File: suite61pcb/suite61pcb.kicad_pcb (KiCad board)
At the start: 2 copper layers, 189.6 x 115.8 mm, 99 parts, among them J1 Battery JST, J2 OLED, J3 FFC_Receiver, SW1 MX_SW_HS, SW10 MX_SW_HS, SW11 MX_SW_HS, SW12 MX_SW_HS, SW13 MX_SW, SW14 MX_SW, SW15 MX_SW_HS, SW16 MX_SW_HS, SW17 MX_SW_HS, SW18 MX_SW_HS, SW19 MX_SW_HS, SW2 MX_SW_HS, SW20 Reset_Button, SW21 MX_SW, SW22 MX_SW, SW23 MX_SW_HS, SW24 MX_SW_HS, SW25 MX_SW_HS, SW26 MX_SW_HS, SW27 MX_SW_HS, SW28 MX_SW_HS, SW29 MX_SW_HS, SW3 MX_SW_HS, SW30 MX_SW_HS, SW31 MX_SW_HS, SW32 MX_SW_HS, SW33 MX_SW_HS, SW34 MX_SW_HS, SW35 MX_SW_HS, SW36 MX_SW_HS, SW37 RotaryEncoder_Switch, SW4 MX_SW_HS, SW5 MX_SW_HS, SW6 MX_SW_HS, SW7 MX_SW_HS, SW8 MX_SW_HS, SW9 MX_SW_HS, U1 nice_nano

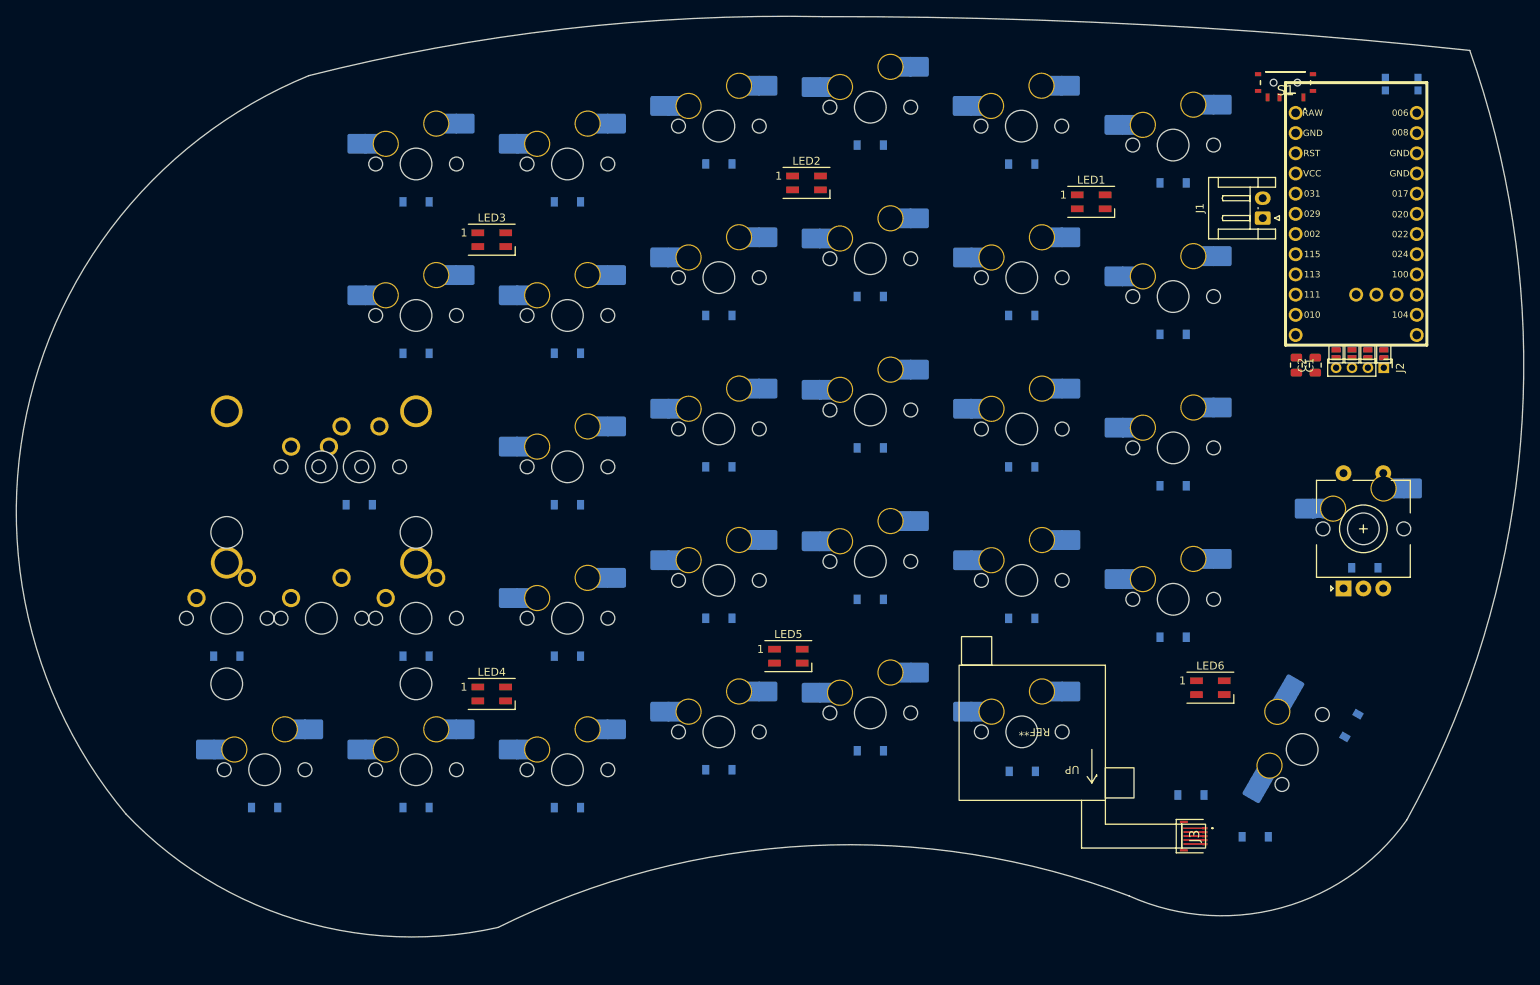
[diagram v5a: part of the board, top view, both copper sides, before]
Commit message: create edge outline
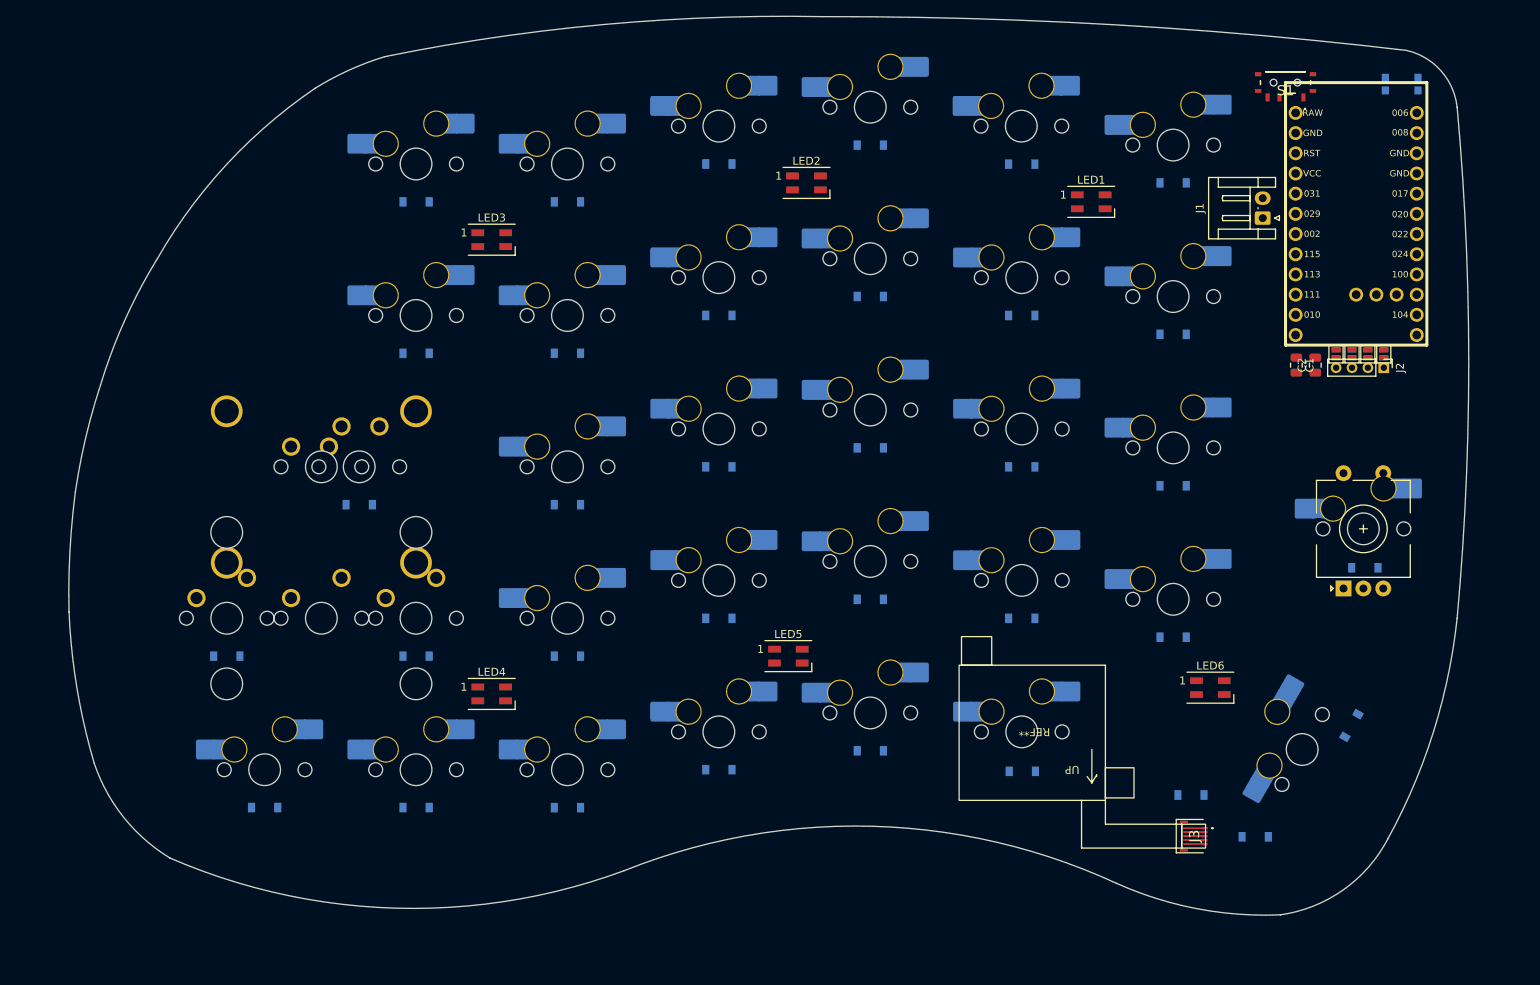
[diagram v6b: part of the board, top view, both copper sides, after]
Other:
- board size 189.6 x 115.8 mm -> 176.1 x 113.1 mm
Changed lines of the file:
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@@
     (fp_arc (start -7 -6.5) (mid -6.853553 -6.853553) (end -6.5 -7) (layer "Eco2.User") (width 0.05))
     (fp_arc (start 6.997236 6.498884) (mid 6.850756 6.852405) (end 6.497236 6.998884) (layer "Eco2.User") (width 0.05))
-    (fp_arc (start 14.780039 -5.999999) (mid 15.133596 -5.853568) (end 15.280039 -5.499999) (layer "Eco2.User") (width 0.05))
+    (fp_arc (start 14.780039 -5.999999) (mid 15.133631 -5.853574) (end 15.280039 -5.499999) (layer "Eco2.User") (width 0.05))
     (fp_arc (start -9.03125 -5.999999) (mid -8.677697 -5.853552) (end -8.53125 -5.499999) (layer "Eco2.User") (width 0.05))
-    (fp_arc (start 9.03125 8.000001) (mid 8.677664 7.853572) (end 8.53125 7.500001) (layer "Eco2.User") (width 0.05))
+    (fp_arc (start 9.03125 8.000001) (mid 8.677699 7.853566) (end 8.53125 7.500001) (layer "Eco2.User") (width 0.05))
     (fp_arc (start -8.53125 7.500001) (mid -8.677697 7.853554) (end -9.03125 8.000001) (layer "Eco2.User") (width 0.05))
     (fp_arc (start 6.5 -7) (mid 6.853553 -6.853553) (end 7 -6.5) (layer "Eco2.User") (width 0.05))
-    (fp_arc (start 8.53125 -5.499999) (mid 8.677738 -5.853509) (end 9.03125 -5.999999) (layer "Eco2.User") (width 0.05))
-    (fp_arc (start 15.28125 7.500001) (mid 15.134777 7.853542) (end 14.78125 8.000001) (layer "Eco2.User") (width 0.05))
+    (fp_arc (start 8.53125 -5.499999) (mid 8.677741 -5.853506) (end 9.03125 -5.999999) (layer "Eco2.User") (width 0.05))
+    (fp_arc (start 15.28125 7.500001) (mid 15.134771 7.853507) (end 14.78125 8.000001) (layer "Eco2.User") (width 0.05))
     (fp_arc (start -6.5 7) (mid -6.853553 6.853553) (end -7 6.5) (layer "Eco2.User") (width 0.05))
     (fp_arc (start -15.28125 -5.499999) (mid -15.134803 -5.853552) (end -14.78125 -5.999999) (layer "Eco2.User") (width 0.05))
@@
     (fp_arc (start -9.03125 -5.999999) (mid -8.677697 -5.853552) (end -8.53125 -5.499999) (layer "Eco2.User") (width 0.05))
     (fp_arc (start -7 -6.5) (mid -6.853553 -6.853553) (end -6.5 -7) (layer "Eco2.User") (width 0.05))
-    (fp_arc (start 8.53125 -5.499999) (mid 8.677738 -5.853509) (end 9.03125 -5.999999) (layer "Eco2.User") (width 0.05))
+    (fp_arc (start 8.53125 -5.499999) (mid 8.677741 -5.853506) (end 9.03125 -5.999999) (layer "Eco2.User") (width 0.05))
     (fp_arc (start -14.78125 8.000001) (mid -15.134803 7.853554) (end -15.28125 7.500001) (layer "Eco2.User") (width 0.05))
     (fp_arc (start -8.53125 7.500001) (mid -8.677697 7.853554) (end -9.03125 8.000001) (layer "Eco2.User") (width 0.05))
-    (fp_arc (start 15.28125 7.500001) (mid 15.134777 7.853542) (end 14.78125 8.000001) (layer "Eco2.User") (width 0.05))
-    (fp_arc (start 9.03125 8.000001) (mid 8.677664 7.853572) (end 8.53125 7.500001) (layer "Eco2.User") (width 0.05))
+    (fp_arc (start 15.28125 7.500001) (mid 15.134771 7.853507) (end 14.78125 8.000001) (layer "Eco2.User") (width 0.05))
+    (fp_arc (start 9.03125 8.000001) (mid 8.677699 7.853566) (end 8.53125 7.500001) (layer "Eco2.User") (width 0.05))
     (fp_arc (start 6.5 -7) (mid 6.853553 -6.853553) (end 7 -6.5) (layer "Eco2.User") (width 0.05))
-    (fp_arc (start 14.780039 -5.999999) (mid 15.133596 -5.853568) (end 15.280039 -5.499999) (layer "Eco2.User") (width 0.05))
+    (fp_arc (start 14.780039 -5.999999) (mid 15.133631 -5.853574) (end 15.280039 -5.499999) (layer "Eco2.User") (width 0.05))
     (fp_arc (start 6.997236 6.498884) (mid 6.850756 6.852405) (end 6.497236 6.998884) (layer "Eco2.User") (width 0.05))
     (fp_line (start -7 -7) (end -7 7) (layer "F.CrtYd") (width 0.05))
@@
     (fp_arc (start -4.864824 3.20022) (mid -4.718377 2.846667) (end -4.364824 2.70022) (layer "B.SilkS") (width 0.15))
     (fp_arc (start 2.494322 0.86022) (mid 1.670693 2.183637) (end 0.2 2.70022) (layer "B.SilkS") (width 0.15))
-    (fp_arc (start 6.085176 4.75022) (mid 5.499393 6.164437) (end 4.085176 6.75022) (layer "B.SilkS") (width 0.15))
+    (fp_arc (start 6.085176 4.75022) (mid 5.499392 6.164435) (end 4.085176 6.75022) (layer "B.SilkS") (width 0.15))
     (fp_line (start 9.525 -9.525) (end -9.525 -9.525) (layer "Dwgs.User") (width 0.12))
     (fp_line (start -9.525 -9.525) (end -9.525 9.525) (layer "Dwgs.User") (width 0.12))
@@
     (fp_line (start -4.864824 3.87022) (end -4.864824 2.70022) (layer "B.CrtYd") (width 0.05))
     (fp_arc (start 2.494322 0.86022) (mid 1.670502 2.183399) (end 0.2 2.70022) (layer "B.CrtYd") (width 0.05))
-    (fp_arc (start 6.085176 4.75022) (mid 5.499393 6.164437) (end 4.085176 6.75022) (layer "B.CrtYd") (width 0.05))
+    (fp_arc (start 6.085176 4.75022) (mid 5.499392 6.164435) (end 4.085176 6.75022) (layer "B.CrtYd") (width 0.05))
     (fp_line (start 7 -7) (end -7 -7) (layer "F.CrtYd") (width 0.05))
     (fp_line (start 7 7) (end 7 -7) (layer "F.CrtYd") (width 0.05))
@@
     )
   )
-  (gr_arc (start 77.7875 29.36875) (mid 109.85027 23.503504) (end 142.407734 21.943379) (layer "Edge.Cuts") (width 0.1))
-  (gr_arc (start 101.6 136.525) (mid 140.87251 126.240817) (end 180.975 132.55625) (layer "Edge.Cuts") (width 0.1))
-  (gr_arc (start 223.8375 26.19375) (mid 230.2357 75.462248) (end 215.9 123.03125) (layer "Edge.Cuts") (width 0.1))
-  (gr_arc (start 142.407734 21.943379) (mid 183.180106 22.967167) (end 223.8375 26.19375) (layer "Edge.Cuts") (width 0.1))
-  (gr_arc (start 101.6 136.525) (mid 76.2977 135.56535) (end 54.76875 122.2375) (layer "Edge.Cuts") (width 0.1))
-  (gr_arc (start 54.76875 122.2375) (mid 42.729925 69.966391) (end 77.7875 29.36875) (layer "Edge.Cuts") (width 0.1))
-  (gr_arc (start 215.9 123.03125) (mid 200.144306 134.052039) (end 180.975 132.55625) (layer "Edge.Cuts") (width 0.1))
+  (gr_arc (start 87.3125 26.9875) (mid 114.72134 22.949627) (end 142.407734 21.943379) (layer "Edge.Cuts") (width 0.1))
+  (gr_arc (start 117.475 129.38125) (mid 148.594878 123.793501) (end 179.3875 130.96875) (layer "Edge.Cuts") (width 0.1))
+  (gr_arc (start 200.025 134.937499) (mid 189.474505 134.1582) (end 179.3875 130.96875) (layer "Edge.Cuts") (width 0.1))
+  (gr_arc (start 222.25 33.3375) (mid 223.712399 65.484375) (end 222.25 97.63125) (layer "Edge.Cuts") (width 0.1))
+  (gr_arc (start 51.59375 68.2625) (mid 54.656291 60.0958) (end 58.7375 52.3875) (layer "Edge.Cuts") (width 0.1))
+  (gr_arc (start 47.625 96.8375) (mid 47.734002 89.281724) (end 48.41875 81.75625) (layer "Edge.Cuts") (width 0.1))
+  (gr_arc (start 215.9 26.19375) (mid 220.214435 28.752794) (end 222.25 33.3375) (layer "Edge.Cuts") (width 0.1))
+  (gr_arc (start 142.407734 21.943379) (mid 179.217334 22.971178) (end 215.9 26.19375) (layer "Edge.Cuts") (width 0.1))
+  (gr_arc (start 78.58125 30.95625) (mid 82.819052 28.690663) (end 87.3125 26.9875) (layer "Edge.Cuts") (width 0.1))
+  (gr_arc (start 117.475 129.38125) (mid 88.746849 134.100947) (end 60.325 127.79375) (layer "Edge.Cuts") (width 0.1))
+  (gr_arc (start 48.41875 81.75625) (mid 49.71695 74.941304) (end 51.59375 68.2625) (layer "Edge.Cuts") (width 0.1))
+  (gr_arc (start 60.325 127.79375) (mid 54.50891 122.6835) (end 50.8 115.8875) (layer "Edge.Cuts") (width 0.1))
+  (gr_arc (start 58.7375 52.3875) (mid 67.441824 40.544518) (end 78.58125 30.95625) (layer "Edge.Cuts") (width 0.1))
+  (gr_arc (start 50.8 115.8875) (mid 48.628743 106.459793) (end 47.625 96.8375) (layer "Edge.Cuts") (width 0.1))
+  (gr_arc (start 222.25 97.63125) (mid 219.262748 111.955078) (end 213.51875 125.4125) (layer "Edge.Cuts") (width 0.1))
+  (gr_arc (start 213.51875 125.4125) (mid 207.921299 131.803351) (end 200.025 134.9375) (layer "Edge.Cuts") (width 0.1))
 )

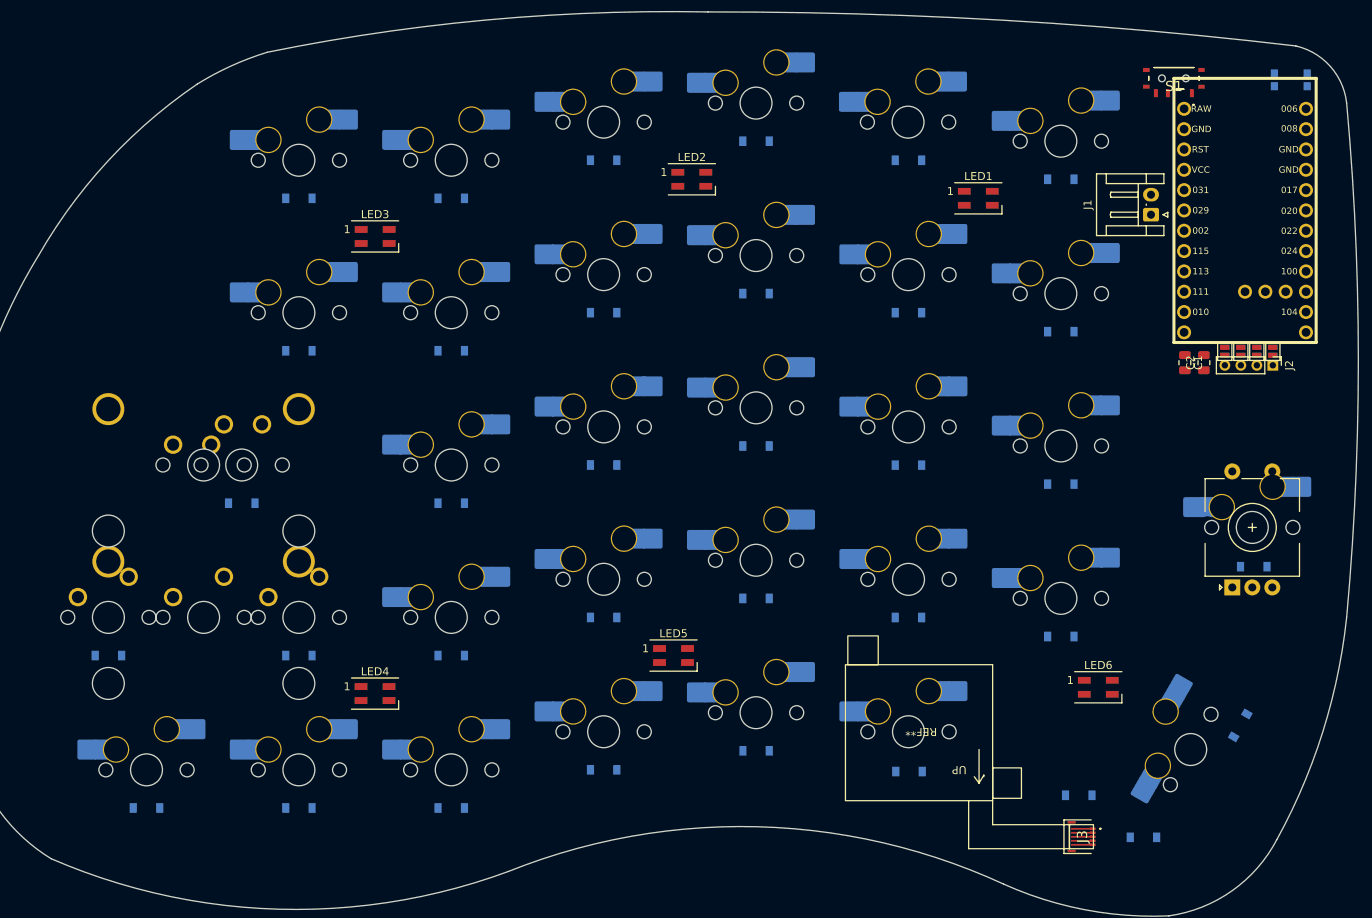
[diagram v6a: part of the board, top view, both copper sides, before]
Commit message: update pcb
check if oled header is right
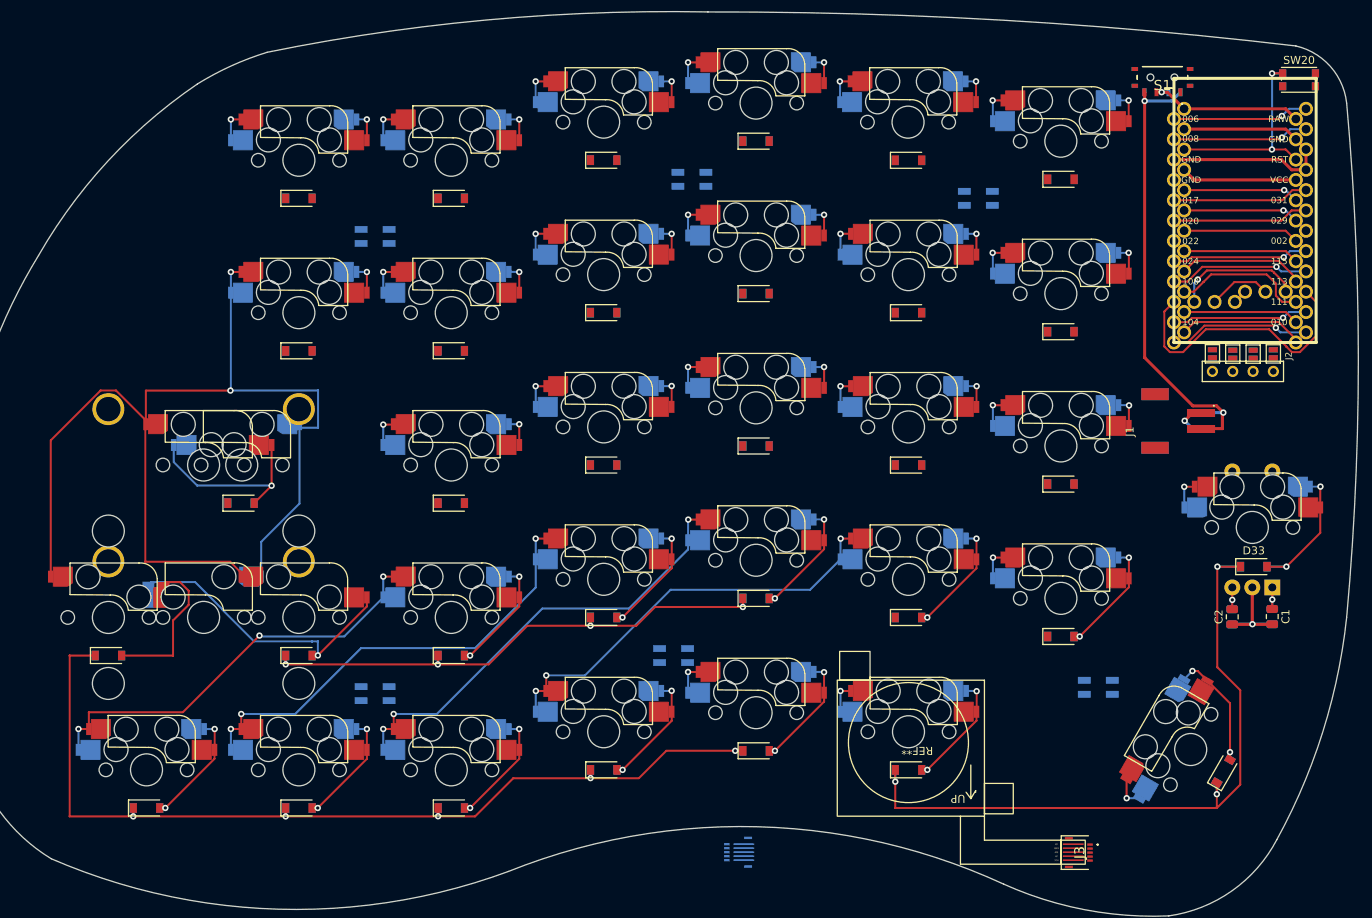
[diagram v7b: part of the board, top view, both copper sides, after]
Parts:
- removed the D31 at (188.8, 119.9)
- removed D34: 1N4148W, Diode_SMD:D_SOD-123
- added J3: FFC_Receiver, LIB_503480-0500:5034800500, B.Cu at (146.4, 127.0)
- added REF**: joycon joystick, suite61:joycon joystick, B.Cu at (158.2, 111.5)
- D1, D10, D11, D12, D13, D14, D15, D16, D17, D18, D19, D2, D20, D21, D22, D23, D24, D25, D26, D27, D28, D29, D3, D30, D4, D5, D6, D7, D8, D9: footprint Diode_SMD:D_SOD-123 -> suite61:D_SOD-123
- D31: renamed from D32; footprint Diode_SMD:D_SOD-123 -> suite61:D_SOD-123
- D32: renamed from D33; footprint Diode_SMD:D_SOD-123 -> suite61:D_SOD-123
- D33: renamed from D35; footprint Diode_SMD:D_SOD-123 -> suite61:D_SOD-123; moved to F.Cu
- J1: footprint Connector_JST:JST_EH_S2B-EH_1x02_P2.50mm_Horizontal -> suite61:JST_S2B-PH-SM4-TB
- J2: footprint Connector_PinHeader_2.00mm:PinHeader_1x04_P2.00mm_Vertical -> SofleKeyboard-footprint:OLED_4Pin
- JP1, JP2, JP3, JP4, LED1, LED2, LED3, LED4, LED5, LED6, SW37: moved to B.Cu
- JP5, JP6, JP7, JP8, SW20: moved to F.Cu
- REF**: value 2-way joystick switch -> joycon joystick; footprint suite61:2-way joystick switch -> suite61:joycon joystick
- SW1, SW10, SW11, SW12, SW15, SW16, SW17, SW18, SW19, SW2, SW23, SW24, SW25, SW26, SW27, SW29, SW3, SW30, SW31, SW32, SW33, SW4, SW5, SW6, SW8, SW9: footprint marbastlib-mx:SW_MX_HS_1u -> suite61:CherryMX_Hotswap; moved to F.Cu
- SW13: footprint marbastlib-mx:SW_MX_1.75u -> suite61:SW_MX_HS_1.75u_1side; moved to B.Cu
- SW14: footprint suite61:SW_MX_P_2.25u -> suite61:STAB_MX_P__HS_2.25u_1side
- SW21: footprint suite61:SW_MX_P_2.25u -> suite61:STAB_MX_P__HS_2.25u_1side; moved to B.Cu
- SW22: footprint marbastlib-mx:SW_MX_1u -> suite61:CherryMX_Hotswap
- SW28: footprint marbastlib-mx:SW_MX_HS_1u -> suite61:CherryMX_Hotswap_1.5; moved to F.Cu
- SW34: footprint marbastlib-mx:SW_MX_1.5u -> suite61:CherryMX_Hotswap
- SW35, SW7: footprint marbastlib-mx:SW_MX_HS_1.5u -> suite61:CherryMX_Hotswap_1.5; moved to F.Cu
- SW36: footprint marbastlib-mx:SW_MX_HS_1u -> suite61:CherryMX_Hotswap
- U1: footprint nice-nano-kicad-master:nice_nano -> suite61:nice_nano
- moved SW34 101.0 mm to (167.5, 111.9)
- moved D31 101.0 mm to (167.5, 116.7)
- moved C1 33.6 mm to (212.9, 97.5)
- moved C2 32.0 mm to (207.9, 97.5)
- moved J1 26.5 mm to (204.1, 73.1)
- moved SW28 19.6 mm to (67.5, 97.6), turned to 0 degrees
- moved D25 19.6 mm to (67.5, 102.4)
- moved SW31 19.6 mm to (110.3, 116.7), turned to 0 degrees
- moved D28 19.6 mm to (110.3, 121.4)
- moved D30 19.3 mm to (148.4, 114.3)
- moved SW33 19.2 mm to (148.4, 109.5), turned to 0 degrees
- moved D29 19.2 mm to (129.4, 116.7)
- moved SW32 19.2 mm to (129.4, 111.9), turned to 0 degrees
- moved D26 19.0 mm to (72.2, 121.4)
- moved SW29 19.0 mm to (72.2, 116.7), turned to 0 degrees
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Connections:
- J3 pad 3: Net-(D34-Pad2) -> JSBTN
- U1 pad 2: unconnected-(U1-Pad2) -> DATA
- U1 pad 31: Enc0 -> JSBTN
- U1 pad 33: unconnected-(U1-Pad33) -> Enc0
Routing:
- net col5: track 0.00 -> 155.0 mm, vias 0 -> 4
- net row4: track 0.00 -> 135.0 mm, vias 0 -> 5
- net row5: track 0.00 -> 105.4 mm, vias 0 -> 3
- net col3: track 0.00 -> 102.9 mm, vias 0 -> 6
- net col2: track 0.00 -> 89.3 mm, vias 0 -> 8
- net row3: track 0.00 -> 86.0 mm, vias 0 -> 4
- net col1: track 0.00 -> 85.9 mm, vias 0 -> 8
- net col4: track 0.00 -> 81.5 mm, vias 0 -> 7
- net GND: track 0.00 -> 58.9 mm, vias 0 -> 2
- net Net-(J1-Pad2): track 0.00 -> 57.4 mm, vias 0 -> 2
- net Net-(D19-Pad2): track 0.00 -> 37.4 mm, vias 0 -> 1
- net RESET: track 0.00 -> 26.7 mm, vias 0 -> 2
- net Net-(D13-Pad2): track 0.00 -> 23.8 mm, vias 0 -> 1
- net col0: track 0.00 -> 23.5 mm, vias 0 -> 6
- net BATTERY: track 0.00 -> 19.7 mm, vias 0 -> 1
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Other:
- board text added: "battery: 98x80x1.5"
